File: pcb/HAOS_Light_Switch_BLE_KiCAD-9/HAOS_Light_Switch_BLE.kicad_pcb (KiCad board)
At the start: 2 copper layers, 30.1 x 29.9 mm, 36 parts, among them J1 GPIO, J2 GPIO, J3 GPIO, J4 Battery_CR2032, J5 PWR, J7 SWD, SW1 SW_Push, SW2 SW_Push, SW3 SW_Push, U1 nrf52832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

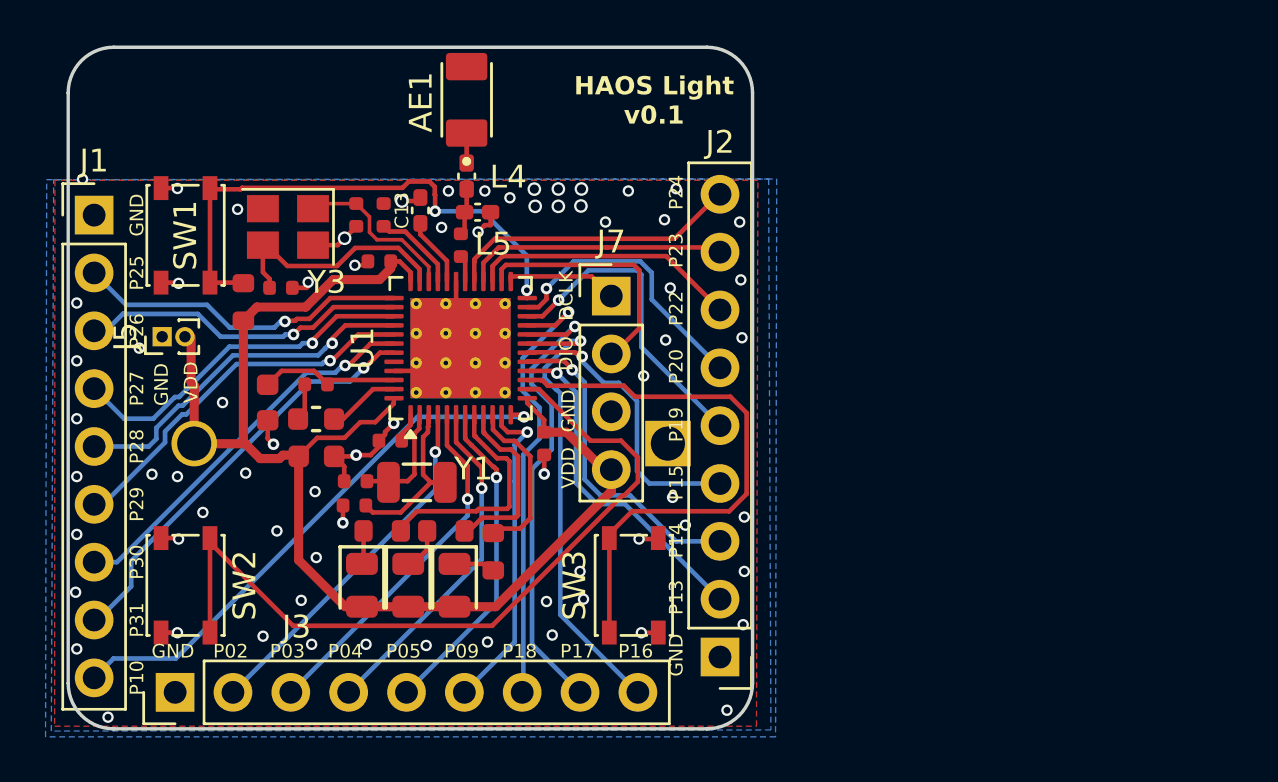
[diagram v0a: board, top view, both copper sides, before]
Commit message: added Tag-Connect programming connector
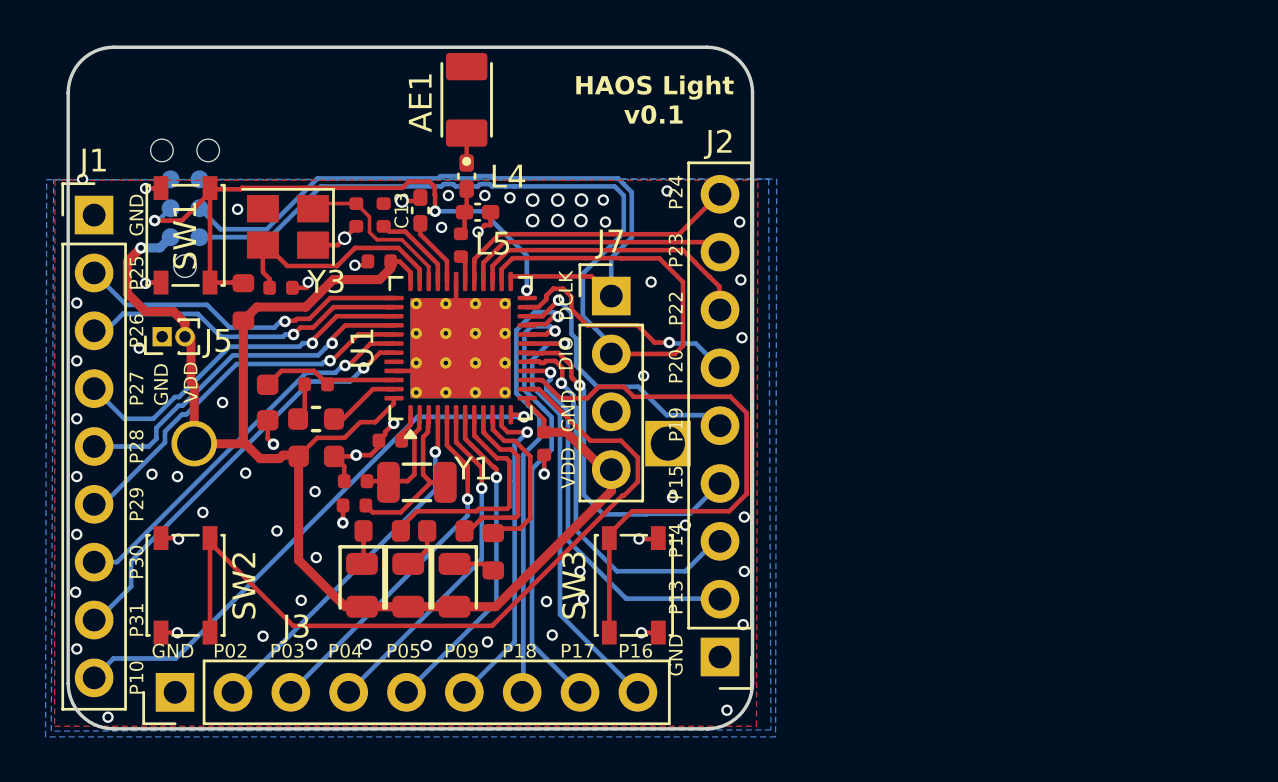
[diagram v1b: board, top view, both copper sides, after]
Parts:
- added J6: Conn_ARM_SWD_TagConnect_TC2030-NL, Connector:Tag-Connect_TC2030-IDC-NL_2x03_P1.27mm_Vertical, B.Cu at (168.6, 111.5)
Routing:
- net /SWDIO: track 10.9 -> 43.2 mm
- net /SWDCLK: track 5.10 -> 30.7 mm
- net VDD: track 61.5 -> 68.9 mm, vias 0 -> 1
- net /RESET: track 23.6 -> 27.6 mm, vias 2 -> 3
- net /P0.14: track 14.3 -> 16.8 mm
- net /P0.15: track 12.8 -> 15.0 mm
- net /P0.19: track 14.0 -> 12.3 mm
- net /P0.13: track 15.0 -> 16.6 mm
- net /P0.20: track 12.2 -> 10.7 mm
- net /P0.22: track 11.8 -> 12.6 mm
- net /P0.16: track 20.4 -> 19.9 mm
- net GND: track 24.4 -> 24.2 mm, vias 71 -> 69
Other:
- board text added: "RESET"
- board text added: "SCLK"
- board text added: "SWIO"

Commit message: Added C4 to help mitigate brown out potential during radio transmissions.
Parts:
- added C4: 47uF, PCM_JLCPCB:C_0805, F.Cu at (172.4, 124.1)

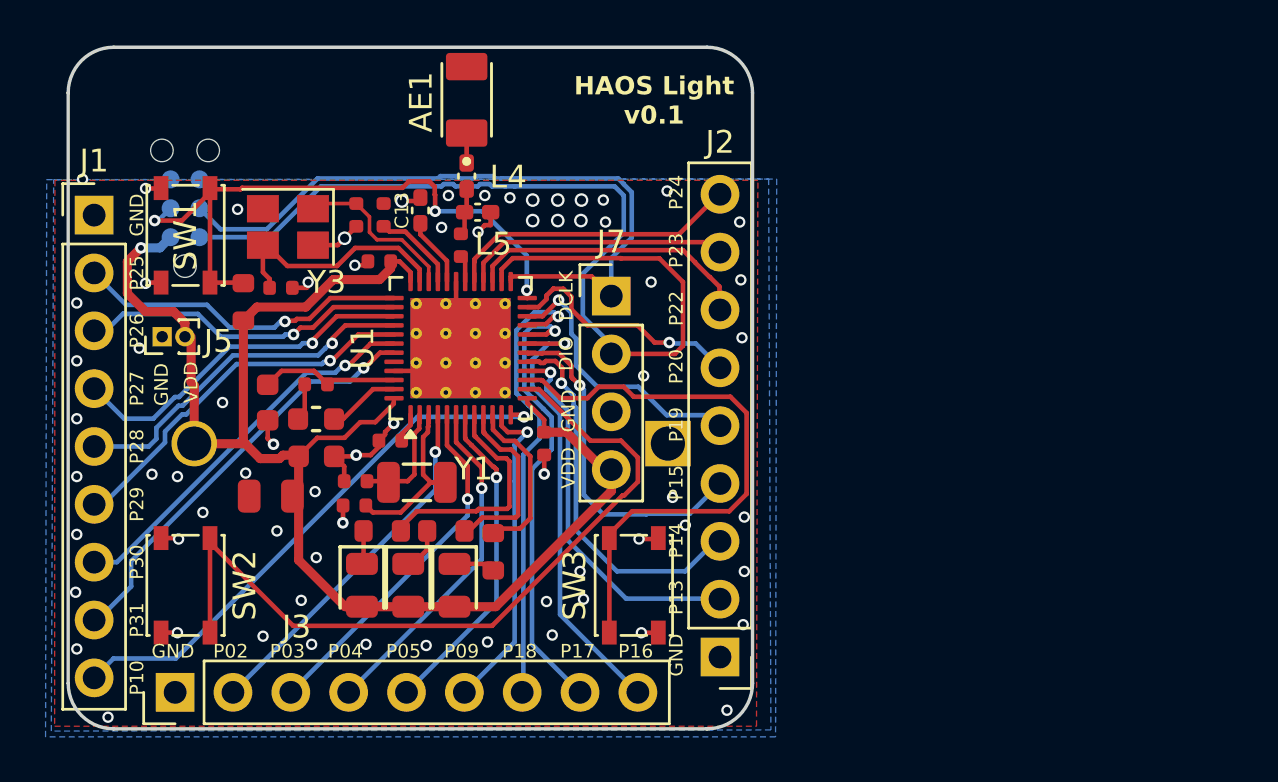
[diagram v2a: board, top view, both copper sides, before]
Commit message: Added SWO to Tag-Connect
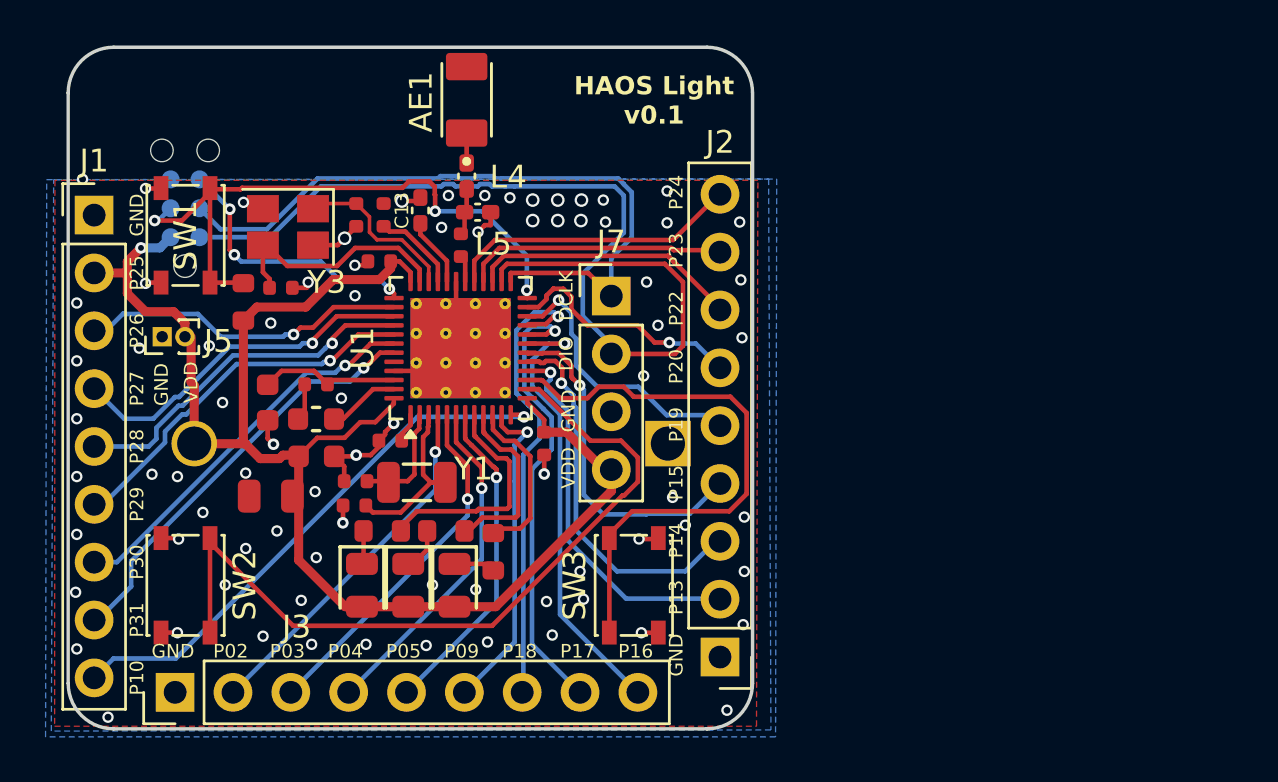
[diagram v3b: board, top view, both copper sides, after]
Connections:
- J1 pad 2: /P0.25 -> VDD
- J6 pad 6: unconnected-(J6-SWO-Pad6) -> /SWO
- U1 pad 37: /P0.25 -> /SWO
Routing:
- net /P0.25: track 14.7 -> 0.00 mm, vias 1 -> 0
- net /SWO: track 0.00 -> 11.9 mm, vias 0 -> 3
- net VDD: track 68.9 -> 70.3 mm
- net GND: vias 69 -> 79

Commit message: Draft AC power sniffer
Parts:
- added C14: 100n, Capacitor_SMD:C_0603_1608Metric, F.Cu at (205.1, 122.5)
- added C15: 10u, Capacitor_SMD:C_0603_1608Metric, B.Cu at (203.2, 128.2)
- added C16: 100n, Capacitor_SMD:C_0603_1608Metric, B.Cu at (202.6, 117.5)
- added D4: MBR0530, Diode_SMD:D_SOD-123, B.Cu at (207.3, 125.7)
- added D5: MBR0530, Diode_SMD:D_SOD-123, F.Cu at (208.3, 118.2)
- added D6: MBR0530, Diode_SMD:D_SOD-123, F.Cu at (208.3, 128.2)
- added D7: MBR0530, Diode_SMD:D_SOD-123, B.Cu at (208.3, 118.7)
- added D8: MBR0530, Diode_SMD:D_SOD-123, B.Cu at (208.3, 128.2)
- added R10: 0R, Resistor_SMD:R_0603_1608Metric, F.Cu at (202.6, 125.7)
- added R11: 100, Resistor_SMD:R_0603_1608Metric, B.Cu at (205.1, 120.0)
- added R12: 0R, Resistor_SMD:R_0603_1608Metric, F.Cu at (203.9, 119.4)
- added R5: 10K, Resistor_SMD:R_0603_1608Metric, B.Cu at (209.6, 123.8)
- added R6: 10K, Resistor_SMD:R_0603_1608Metric, B.Cu at (205.8, 123.0)
- added R7: 10K, Resistor_SMD:R_0603_1608Metric, B.Cu at (209.0, 121.9)
- added R8: 1K, Resistor_SMD:R_0603_1608Metric, B.Cu at (201.3, 128.2)
- added R9: 0R, Resistor_SMD:R_0603_1608Metric, F.Cu at (202.0, 120.0)
- added TP19: CONN_01, Connector_PinHeader_1.00mm:PinHeader_1x01_P1.00mm_Vertical, F.Cu at (204.5, 126.8)
- added TP20: CONN_01, Connector_PinHeader_1.00mm:PinHeader_1x01_P1.00mm_Vertical, F.Cu at (202.6, 116.2)
- added U2: ZMCT103C, easyeda2kicad:XFMR-TH_ZMCT103C, B.Cu at (205.1, 122.7)
- added U3: TP4056, easyeda2kicad:ESOP-8_L4.9-W3.9-P1.27-LS6.0-BL-EP, F.Cu at (208.3, 123.2)
- added U4: FS8205A, easyeda2kicad:TSSOP-8_L4.4-W3.0-P0.65-LS6.4-BL-2, B.Cu at (202.6, 122.5)
- added U5: DW01, easyeda2kicad:SOT-23-6_L2.9-W1.6-P0.95-LS2.8-BL, F.Cu at (202.6, 123.2)

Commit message: Draft
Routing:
- net Net-(D4-A): track 0.00 -> 21.6 mm, vias 0 -> 3
- net Net-(D4-K): track 0.00 -> 13.9 mm, vias 0 -> 2
- net /BAT-: track 0.00 -> 12.7 mm, vias 0 -> 1
- net Net-(D5-A): track 0.00 -> 7.93 mm
- net Net-(U5-CS): track 0.00 -> 5.27 mm, vias 0 -> 1
- net VDD: track 70.3 -> 75.6 mm
- net Net-(U5-VCC): track 0.00 -> 4.37 mm, vias 0 -> 1
- net GND: track 24.2 -> 28.1 mm
- net /G1: track 0.00 -> 3.30 mm, vias 0 -> 1
- net /SOLAR_STDBY: track 0.00 -> 3.25 mm, vias 0 -> 1
- net /SOLAR_CHRG: track 0.00 -> 2.86 mm, vias 0 -> 1
- net /G2: track 0.00 -> 2.79 mm, vias 0 -> 1
- net /OC: track 0.00 -> 2.71 mm
- net /PROG: track 0.00 -> 2.01 mm, vias 0 -> 1
- net Net-(D6-A): track 0.00 -> 1.68 mm
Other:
- board size 30.1 x 29.9 mm -> 48.5 x 29.9 mm

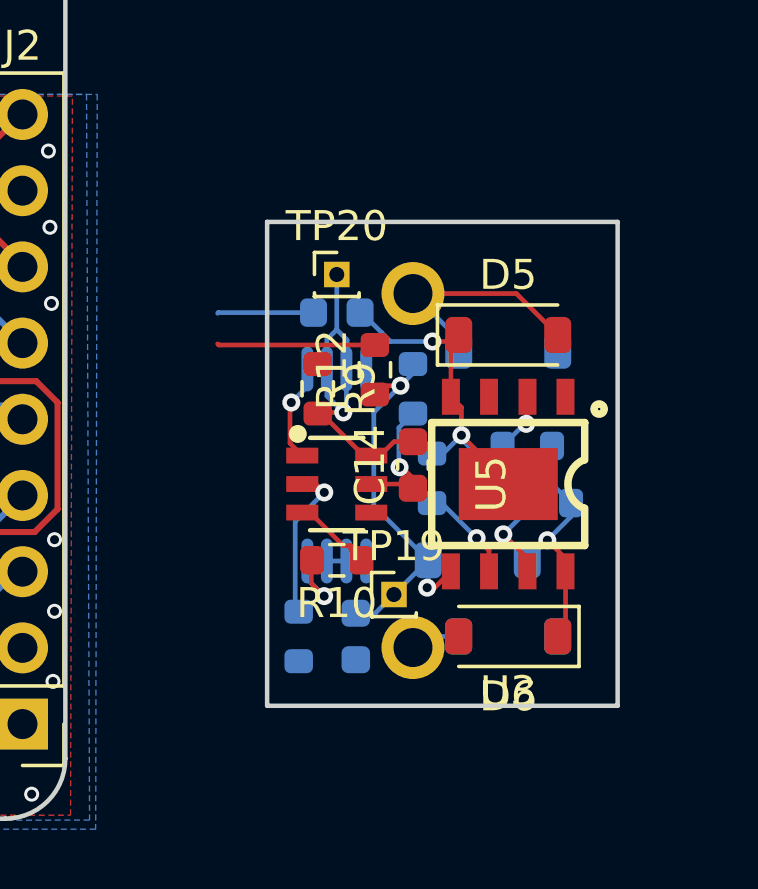
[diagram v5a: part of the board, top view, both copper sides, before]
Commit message: Draft updated trace width
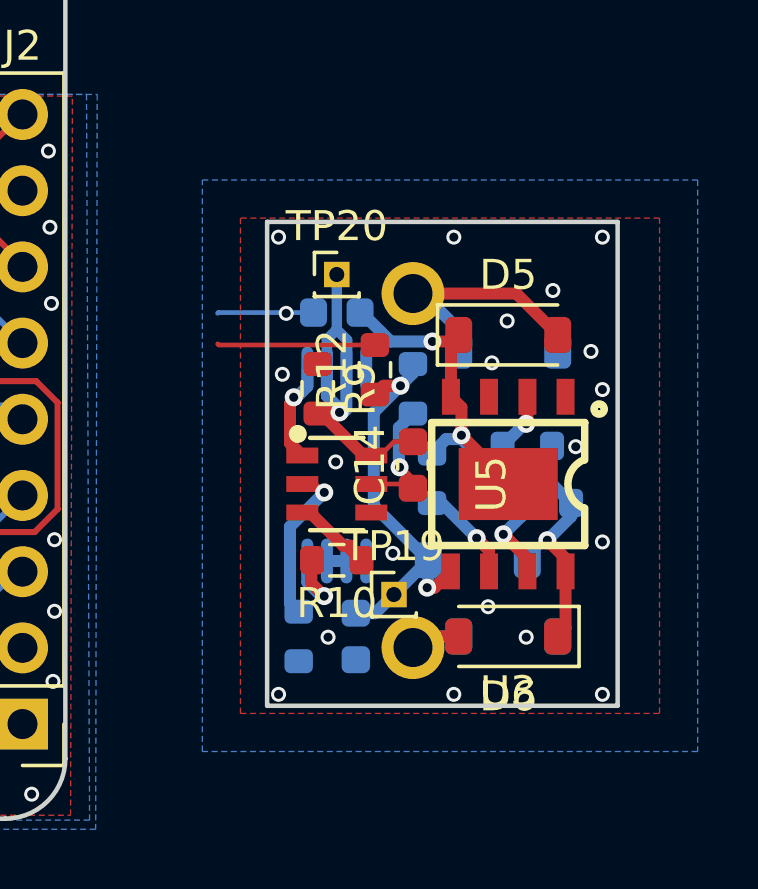
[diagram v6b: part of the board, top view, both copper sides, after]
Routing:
- net Net-(D6-A): track 1.68 -> 3.36 mm
- net GND: vias 79 -> 99

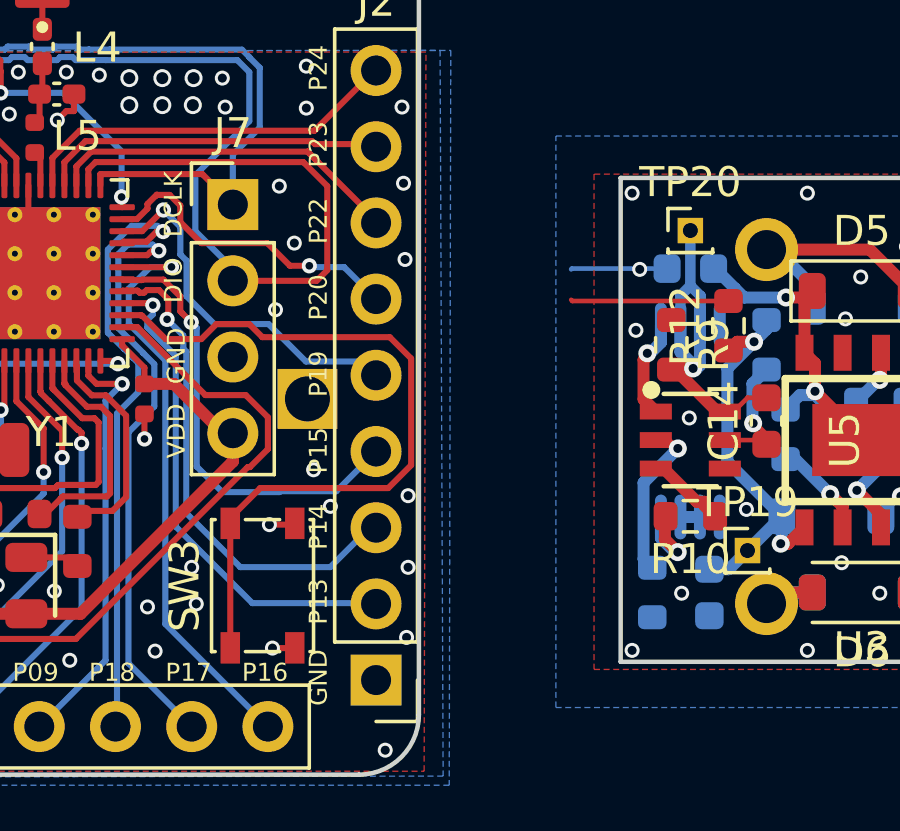
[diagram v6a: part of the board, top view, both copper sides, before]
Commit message: Change R7 limiting charge current to 10ma for LIR2032 charging.
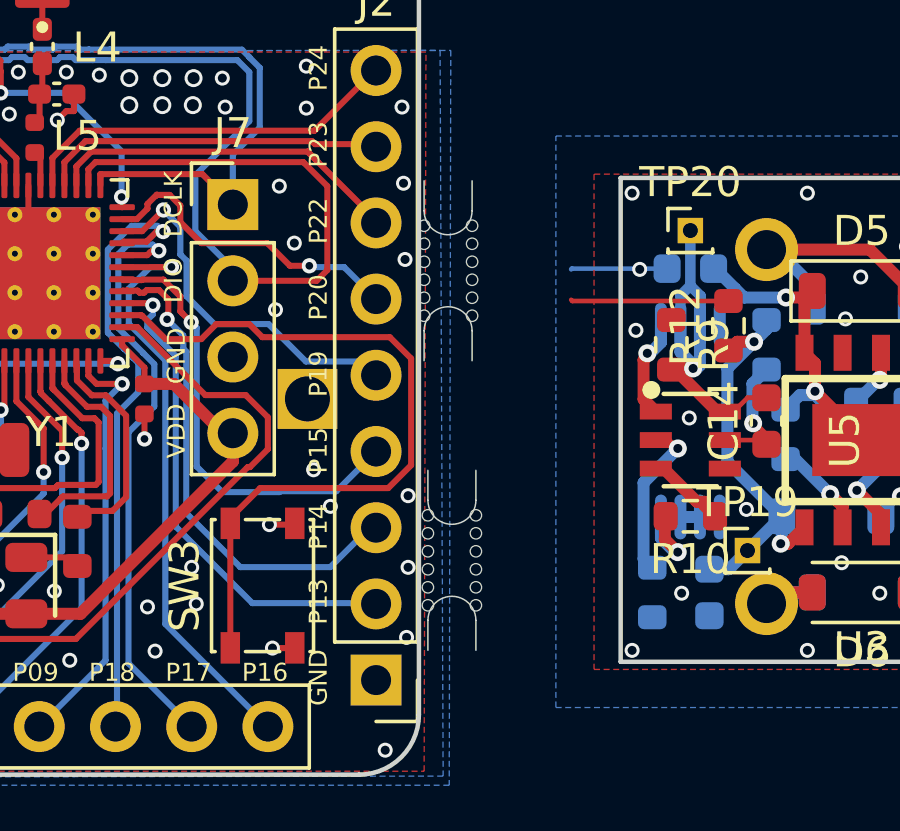
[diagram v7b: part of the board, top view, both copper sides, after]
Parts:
- added M1: ~, PCM_JLCPCB:MouseBites, Cosmetic, JLCPCB, 1.6mm, F.Cu at (193.9, 130.2)
- added M2: ~, PCM_JLCPCB:MouseBites, Cosmetic, JLCPCB, 1.6mm, F.Cu at (193.7, 120.5)
